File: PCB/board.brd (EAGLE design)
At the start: 35 x 50 mm, 9 parts, among them J1 PROG-HEADER_2X3_SHROUDED, J10 PROG-HEADER_2X5_1.27MM-SHROUD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, J2 PROG-HEADER_2X5_2.00MM-SHROUD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, J3 PROG-HEADER_2X5_SHROUDED, J5 PROG-HEADER_2X10_RIGHT-ANGLE, J6 PROG-HEADER_2X10_SHROUDED, J8 CONN-1X4, J9 CONN-1X6

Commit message: connected pin 5, 9 to GND
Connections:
- net GND: now also J10.15, J10.19, J10.5, J10.9, J2.5, J2.9, J3.5, J3.9
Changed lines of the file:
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@@
 <text x="2.667" y="25.146" size="1.524" layer="22" font="vector" ratio="15" rot="MR270" align="center">&gt;GITHUB</text>
 <dimension x1="1" y1="0" x2="18.5" y2="0" x3="9.75" y3="52.5" textsize="1.778" layer="51"/>
+<text x="11.43" y="27.178" size="1.1684" layer="22" font="vector" ratio="15" rot="MR315" align="bottom-right">GND</text>
+<text x="6.35" y="27.178" size="1.1684" layer="22" font="vector" ratio="15" rot="MR315" align="bottom-right">GND</text>
 </plain>
 <attributes>
@@
 <via x="8.89" y="30.734" extent="1-16" drill="0.35"/>
 <via x="4.064" y="46.736" extent="1-16" drill="0.35"/>
+<contactref element="J3" pad="5"/>
+<contactref element="J3" pad="9"/>
+<contactref element="J10" pad="15"/>
+<contactref element="J10" pad="5"/>
+<contactref element="J10" pad="9"/>
+<contactref element="J10" pad="19"/>
+<contactref element="J2" pad="5"/>
+<contactref element="J2" pad="9"/>
 </signal>
 <signal name="RTCK">
@@
 <mfgpreviewcolor name="substratecolor" color="0xFF786E46"/>
 </mfgpreviewcolors>
-<errors>
-</errors>
 </board>
 </drawing>

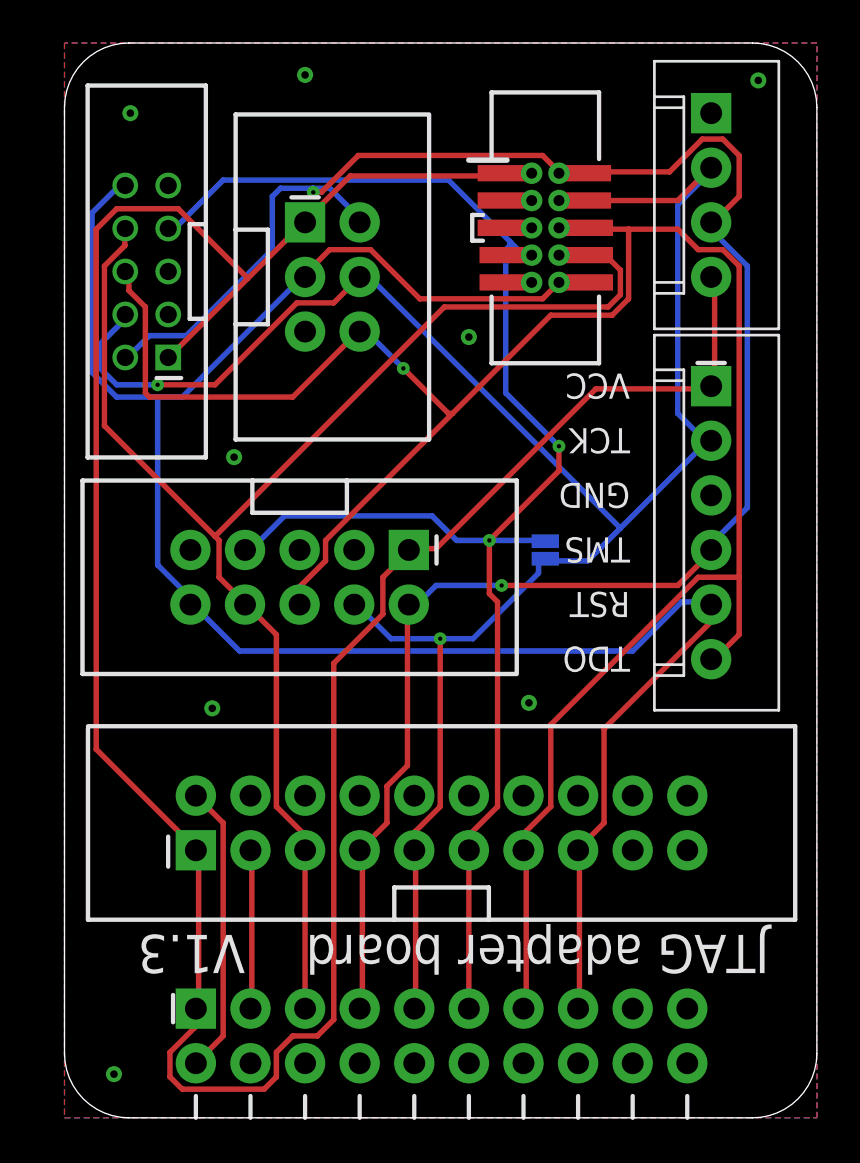
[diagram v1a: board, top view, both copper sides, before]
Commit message: changed right angle connector to end launch
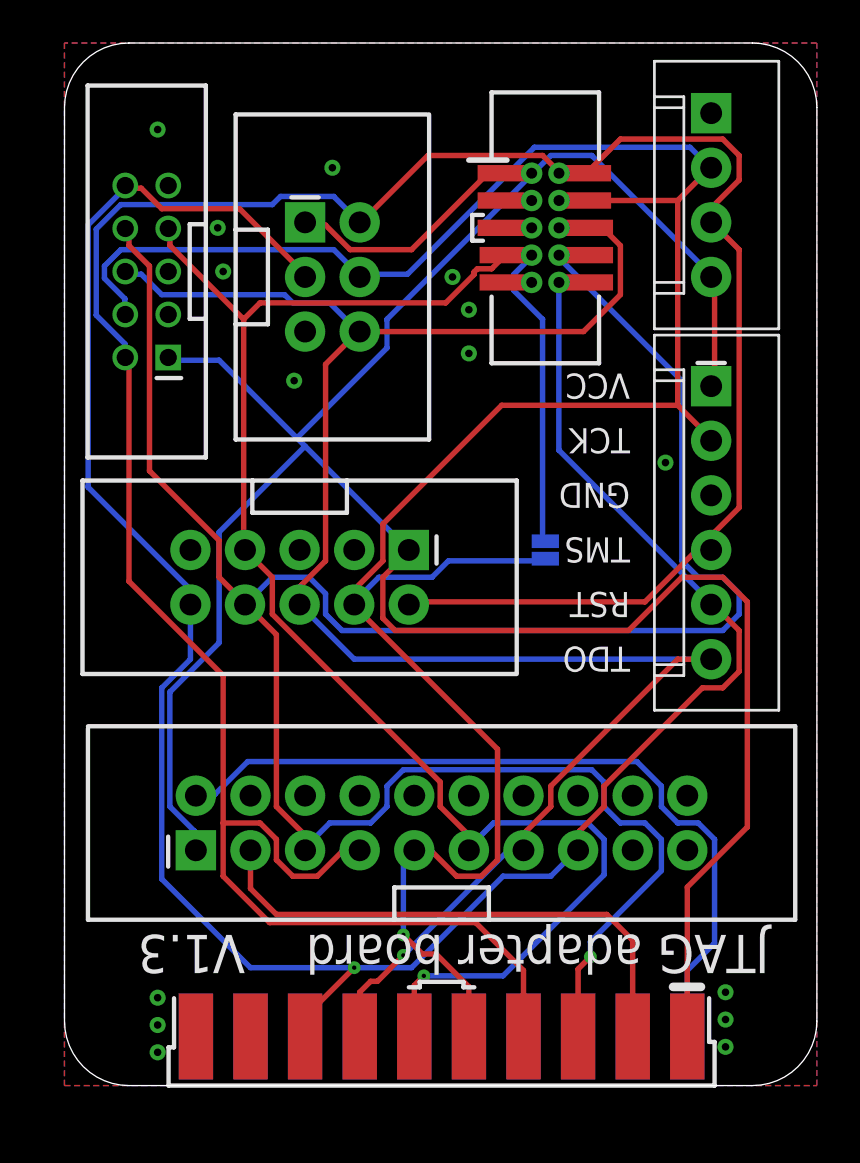
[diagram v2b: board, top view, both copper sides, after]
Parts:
- removed J5: PROG-HEADER_2X10_RIGHT-ANGLE, angrypig7-Connectors-Programming:2X10-2.54MM-RIGHT-ANGLE
- added J4: PROG-HEADER_2X10_2.54MM-END-LAUNCH, angrypig7-Connectors-Programming:2X10-2.54MM-END-LAUNCH
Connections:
- net 2: now also J4.2; no longer J5.2
- net GND: now also J4.10, J4.12, J4.14, J4.16, J4.18, J4.20, J4.4, J4.6, J4.8; no longer J5.10, J5.12, J5.14, J5.16, J5.18, J5.20, J5.4, J5.6, J5.8
- net NTRST: now also J4.3; no longer J5.3
- net RST: now also J4.15; no longer J5.15
- net RTCK: now also J4.11; no longer J5.11
- net TCK: now also J4.9; no longer J5.9
- net TDI: now also J4.5; no longer J5.5
- net TDO: now also J4.13; no longer J5.13
- net TMS: now also J4.7; no longer J5.7
- net VCC: now also J4.1; no longer J5.1
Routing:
- net TDI: track 68.5 -> 111.7 mm, vias 0 -> 1
- net TMS: track 94.0 -> 128.8 mm, vias 2 -> 0
- net 2: track 13.5 -> 36.5 mm
- net TCK: track 95.8 -> 114.2 mm, vias 2 -> 1
- net NTRST: track 7.42 -> 25.0 mm
- net RST: track 95.3 -> 108.0 mm, vias 0 -> 1
- net TDO: track 102.5 -> 91.0 mm
- net RTCK: track 74.7 -> 85.9 mm, vias 2 -> 1
- net VCC: track 127.1 -> 126.4 mm
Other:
- board size 35 x 50 mm -> 35 x 48.5 mm
- board text added: "TCK-RTCK"

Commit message: fixed footprint error
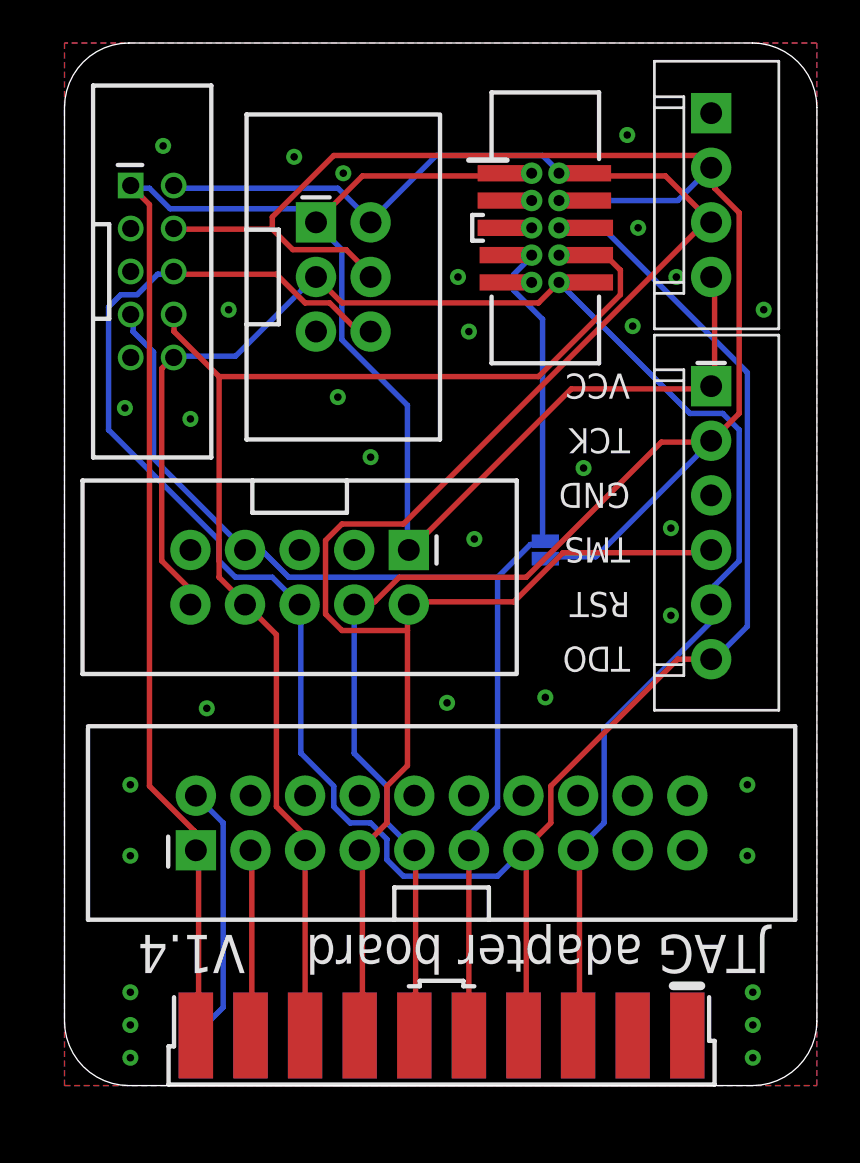
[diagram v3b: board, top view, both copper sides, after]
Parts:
- moved J1 0.51 mm to (14.0, 39.1)
- moved J2 0.25 mm to (5.08, 39.4), turned to 0 degrees
- turned J4 to 90 degrees
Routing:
- net TDI: track 111.7 -> 60.7 mm, vias 1 -> 0
- net TMS: track 128.8 -> 96.4 mm
- net RST: track 108.0 -> 76.5 mm, vias 1 -> 0
- net VCC: track 126.4 -> 100.8 mm
- net 2: track 36.5 -> 12.2 mm
- net RTCK: track 85.9 -> 65.8 mm, vias 1 -> 0
- net NTRST: track 25.0 -> 8.65 mm
- net TDO: track 91.0 -> 103.2 mm, vias 1 -> 0
- net TCK: track 114.2 -> 106.5 mm, vias 1 -> 0

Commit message: V1.5
 - changed RST to TDI for 3*2 pin connector
 - optimized routing
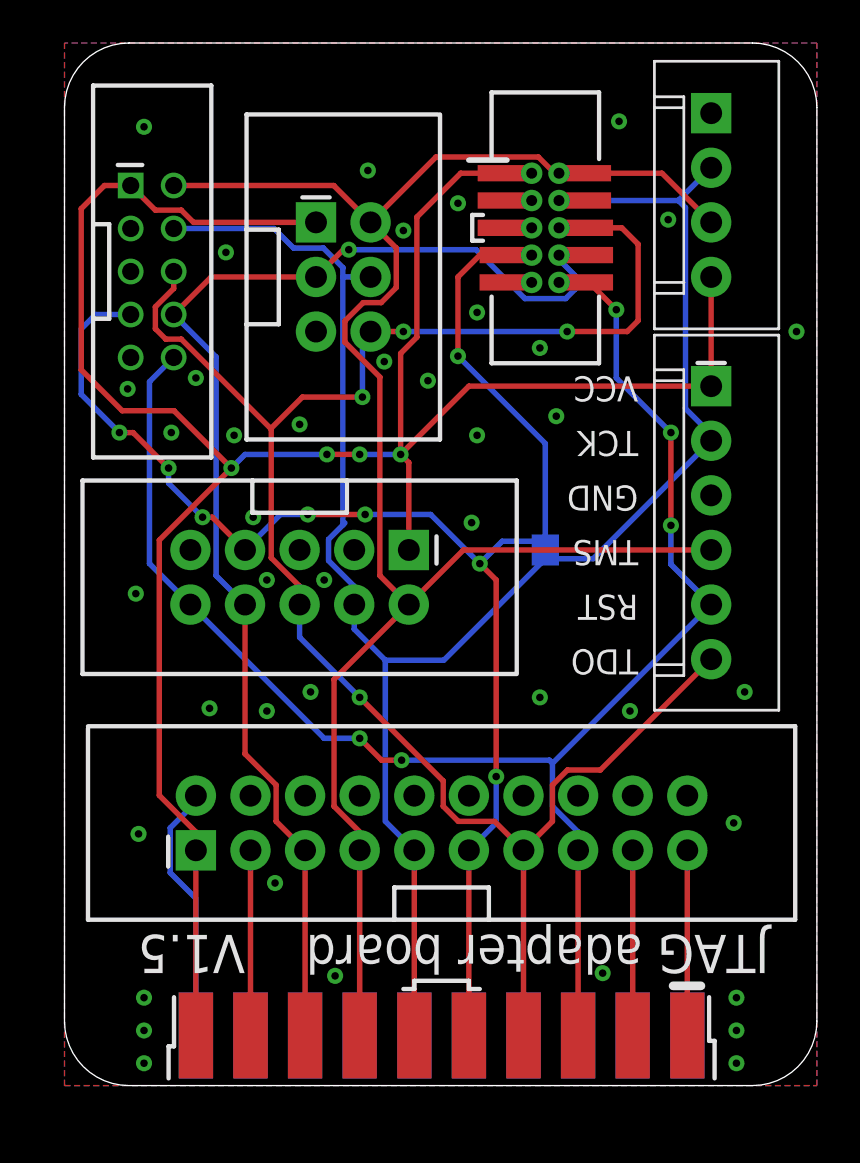
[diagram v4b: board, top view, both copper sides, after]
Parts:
- JP1: device SparkFun-Jumpers:SMT-JUMPER_2_NO_SILK -> angrypig7-Jumpers:SMT-JUMPER_2_NO_SILK
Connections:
- net VCC renamed VREF
- new net 17: J4.17, J6.17
- new net 19: J4.19, J6.19
- net RST: no longer J1.3
- net TDI: now also J1.3
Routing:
- net TCK: track 106.5 -> 86.6 mm
- net TDO: track 103.2 -> 84.8 mm, vias 0 -> 4
- net TMS: track 96.4 -> 85.1 mm
- net 19: track 0.00 -> 8.61 mm
- net 17: track 0.00 -> 8.61 mm
- net RTCK: track 65.8 -> 72.1 mm, vias 0 -> 8
- net VREF: track 100.8 -> 106.7 mm, vias 0 -> 4
- net RST: track 76.5 -> 73.7 mm, vias 0 -> 5
- net TDI: track 60.7 -> 59.0 mm, vias 0 -> 1

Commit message: rollback to V1.4
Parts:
- JP1: device angrypig7-Jumpers:SMT-JUMPER_2_NO_SILK -> SparkFun-Jumpers:SMT-JUMPER_2_NO_SILK
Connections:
- net VREF renamed VCC
- removed net 17: J4.17, J6.17
- removed net 19: J4.19, J6.19
- net RST: now also J1.3
- net TDI: no longer J1.3
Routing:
- net TCK: track 86.6 -> 106.5 mm
- net TDO: track 84.8 -> 103.2 mm, vias 4 -> 0
- net TMS: track 85.1 -> 96.4 mm
- net 19: track 8.61 -> 0.00 mm
- net 17: track 8.61 -> 0.00 mm
- net RTCK: track 72.1 -> 65.8 mm, vias 8 -> 0
- net VCC: track 106.7 -> 100.8 mm, vias 4 -> 0
- net RST: track 73.7 -> 76.5 mm, vias 5 -> 0
- net TDI: track 59.0 -> 60.7 mm, vias 1 -> 0

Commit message: V1.6 update
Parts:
- removed J2: PROG-HEADER_2X5_2.00MM-SHROUDED, angrypig7-Connectors-Programming:2X5-2.00MM-SHROUDED
- removed J6: PROG-HEADER_2X10_SHROUDED, angrypig7-Connectors-Programming:2X10-2.54MM-SHROUDED
- removed J9: CONN-1X6, angrypig7-Connectors-Programming:MOLEX-1X6-2.54MM
- removed JP1: TCK-RTCK, SparkFun-Jumpers:SMT-JUMPER_2_NO_SILK
- added C1: 100nF, angrypig7-RCL:C0603
- added S1: SWITCH-SPST-SMD-5.1MM, angrypig7-Switches:TACTILE_SWITCH_SMD_5.1MM
- J8: device angrypig7-Connectors-Programming:MOLEX-1X4-2.54MM -> angrypig7-Connectors-Programming:XH-4P-2.54MM
- moved J8 24.3 mm to (28.4, 22.6)
- moved J10 23.1 mm to (16.0, 19.6), turned to 180 degrees
- moved J3 14.5 mm to (16.0, 11.2)
- moved J1 10.6 mm to (16.0, 28.7), turned to 270 degrees
- moved J4 3.00 mm to (16.0, 2.25)
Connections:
- net 2: no longer J6.2
- net GND: now also C1.2, S1.3; no longer J2.3, J2.5, J2.9, J6.10, J6.12, J6.14, J6.16, J6.18, J6.20, J6.4, J6.6, J6.8, J9.3
- net NTRST: no longer J6.3
- net RST: now also C1.1, S1.1; no longer J2.10, J6.15, J9.5
- net RTCK: no longer J2.7, J6.11, JP1.2
- net TCK: no longer J2.4, J6.9, J9.2, JP1.1
- net TDI: no longer J2.8, J6.5
- net TDO: no longer J2.6, J6.13, J9.6
- net TMS: no longer J2.2, J6.7, J9.4
- net VCC: no longer J2.1, J6.1, J9.1
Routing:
- net TDO: track 103.2 -> 31.5 mm, vias 0 -> 2
- net TCK: track 106.5 -> 41.3 mm
- net TMS: track 96.4 -> 44.7 mm, vias 0 -> 1
- net TDI: track 60.7 -> 17.0 mm
- net RTCK: track 65.8 -> 27.9 mm, vias 0 -> 3
- net VCC: track 100.8 -> 75.9 mm, vias 0 -> 1
- net 2: track 12.2 -> 0.00 mm
- net RST: track 76.5 -> 65.4 mm, vias 0 -> 1
- net NTRST: track 8.65 -> 0.00 mm
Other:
- board size 35 x 48.5 mm -> 32 x 34 mm
- board text removed: ">CREVISION"
- board text removed: ">GITHUB"
- board text removed: "TCK-RTCK"
